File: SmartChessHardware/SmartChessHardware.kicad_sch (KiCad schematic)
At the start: 26 parts, among them IC1 Pi-Zero-UART, IC2 Arduino_UNO_R3, IC3 MCP23017x-x-SO, J1 Barrel_Jack

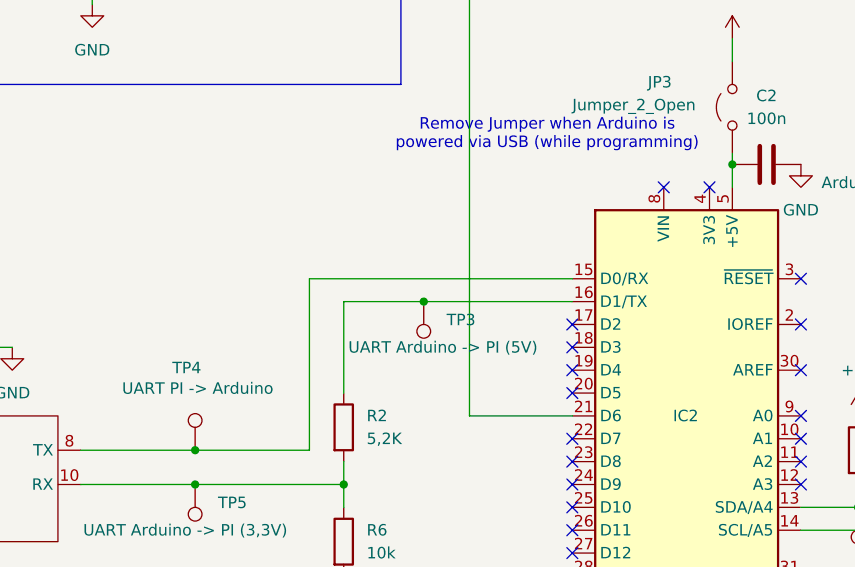
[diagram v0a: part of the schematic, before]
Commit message: Added jumper to disconnect UART
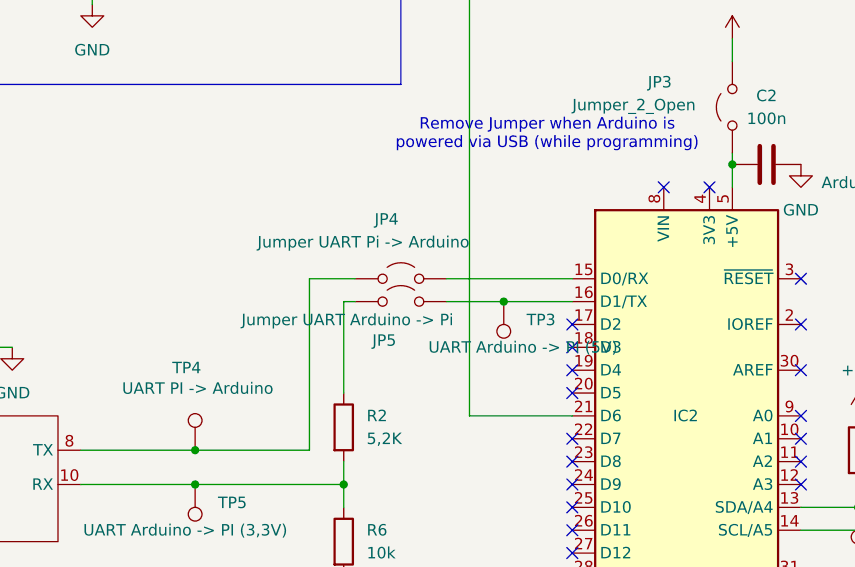
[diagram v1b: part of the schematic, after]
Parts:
- added JP4: Jumper UART Pi -> Arduino, symbol Jumper:Jumper_2_Open
- added JP5: Jumper UART Arduino -> Pi, symbol Jumper:Jumper_2_Open
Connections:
- net at IC1.8 (TX), TP4.1: now also JP4.1 (A); no longer IC2.15 (D0/RX)
- net at IC2.16 (D1/TX), TP3.1: now also JP5.2 (B); no longer R2.1
- new net: JP5.1 (A), R2.1
- new net: IC2.15 (D0/RX), JP4.2 (B)
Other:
- moved on the sheet: TP3
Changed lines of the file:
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@@
 	)
 	(junction
-		(at 114.3 82.55)
+		(at 123.19 82.55)
 		(diameter 0)
 		(color 0 0 0 0)
@@
 	(wire
 		(pts
-			(xy 130.81 82.55) (xy 114.3 82.55)
+			(xy 130.81 82.55) (xy 123.19 82.55)
 		)
 		(stroke
@@
 	(wire
 		(pts
+			(xy 116.84 80.01) (xy 130.81 80.01)
+		)
+		(stroke
+			(width 0)
+			(type default)
+		)
+	)
+	(wire
+		(pts
 			(xy 128.27 113.03) (xy 128.27 135.89)
 		)
@@
 	(wire
 		(pts
-			(xy 101.6 80.01) (xy 130.81 80.01)
+			(xy 101.6 80.01) (xy 106.68 80.01)
 		)
 		(stroke
@@
 	(wire
 		(pts
-			(xy 114.3 82.55) (xy 105.41 82.55)
+			(xy 105.41 82.55) (xy 106.68 82.55)
 		)
 		(stroke
@@
 	(wire
 		(pts
+			(xy 116.84 82.55) (xy 123.19 82.55)
+		)
+		(stroke
+			(width 0)
+			(type default)
+		)
+	)
+	(wire
+		(pts
 			(xy 227.33 105.41) (xy 227.33 115.57)
 		)
@@
 	)
 	(symbol
+		(lib_id "Jumper:Jumper_2_Open")
+		(at 111.76 82.55 0)
+		(unit 1)
+		(body_style 1)
+		(exclude_from_sim no)
+		(in_bom yes)
+		(on_board yes)
+		(in_pos_files yes)
+		(dnp no)
+		(property "Reference" "JP5"
+			(at 111.252 86.868 0)
+			(show_name no)
+			(do_not_autoplace no)
+			(effects
+				(font
+					(size 1.27 1.27)
+				)
+				(justify right)
+			)
+		)
+		(property "Value" "Jumper UART Arduino -> Pi"
+			(at 117.602 84.582 0)
+			(show_name no)
+			(do_not_autoplace no)
+			(effects
+				(font
+					(size 1.27 1.27)
+				)
+				(justify right)
+			)
+		)
+		(property "Footprint" ""
+			(at 111.76 82.55 0)
+			(hide yes)
+			(show_name no)
+			(do_not_autoplace no)
+			(effects
+				(font
+					(size 1.27 1.27)
+				)
+			)
+		)
+		(property "Datasheet" ""
+			(at 111.76 82.55 0)
+			(hide yes)
+			(show_name no)
+			(do_not_autoplace no)
+			(effects
+				(font
+					(size 1.27 1.27)
+				)
+			)
+		)
+		(property "Description" "Jumper, 2-pole, open"
+			(at 111.76 82.55 0)
+			(hide yes)
+			(show_name no)
+			(do_not_autoplace no)
+			(effects
+				(font
+					(size 1.27 1.27)
+				)
+			)
+		)
+		(pin "1"
+		)
+		(pin "2"
+		)
+		(instances
+			(project "SmartChessHardware"
+				(path "/f14972b6-de47-451d-92ca-2832c545b949"
+					(reference "JP5")
+					(unit 1)
+				)
+			)
+		)
+	)
+	(symbol
 		(lib_id "Connector:TestPoint")
 		(at 88.9 102.87 180)
@@
 	)
 	(symbol
+		(lib_id "Jumper:Jumper_2_Open")
+		(at 111.76 80.01 0)
+		(unit 1)
+		(body_style 1)
+		(exclude_from_sim no)
+		(in_bom yes)
+		(on_board yes)
+		(in_pos_files yes)
+		(dnp no)
+		(property "Reference" "JP4"
+			(at 111.506 73.406 0)
+			(show_name no)
+			(do_not_autoplace no)
+			(effects
+				(font
+					(size 1.27 1.27)
+				)
+				(justify right)
+			)
+		)
+		(property "Value" "Jumper UART Pi -> Arduino"
+			(at 119.38 75.946 0)
+			(show_name no)
+			(do_not_autoplace no)
+			(effects
+				(font
+					(size 1.27 1.27)
+				)
+				(justify right)
+			)
+		)
+		(property "Footprint" ""
+			(at 111.76 80.01 0)
+			(hide yes)
+			(show_name no)
+			(do_not_autoplace no)
+			(effects
+				(font
+					(size 1.27 1.27)
+				)
+			)
+		)
+		(property "Datasheet" ""
+			(at 111.76 80.01 0)
+			(hide yes)
+			(show_name no)
+			(do_not_autoplace no)
+			(effects
+				(font
+					(size 1.27 1.27)
+				)
+			)
+		)
+		(property "Description" "Jumper, 2-pole, open"
+			(at 111.76 80.01 0)
+			(hide yes)
+			(show_name no)
+			(do_not_autoplace no)
+			(effects
+				(font
+					(size 1.27 1.27)
+				)
+			)
+		)
+		(pin "1"
+		)
+		(pin "2"
+		)
+		(instances
+			(project "SmartChessHardware"
+				(path "/f14972b6-de47-451d-92ca-2832c545b949"
+					(reference "JP4")
+					(unit 1)
+				)
+			)
+		)
+	)
+	(symbol
 		(lib_id "MCU_Module:Arduino_UNO_R3")
 		(at 143.51 95.25 0)
@@
 	(symbol
 		(lib_id "Connector:TestPoint")
-		(at 114.3 82.55 180)
+		(at 123.19 82.55 180)
 		(unit 1)
 		(body_style 1)
@@
 		(dnp no)
 		(property "Reference" "TP3"
-			(at 116.84 84.5819 0)
+			(at 125.73 84.5819 0)
 			(show_name no)
 			(do_not_autoplace no)
@@
 		)
 		(property "Value" "UART Arduino -> PI (5V)"
-			(at 105.918 87.63 0)
+			(at 114.808 87.63 0)
 			(show_name no)
 			(do_not_autoplace no)
@@
 		)
 		(property "Footprint" ""
-			(at 109.22 82.55 0)
+			(at 118.11 82.55 0)
 			(hide yes)
 			(show_name no)
@@
 		)
 		(property "Datasheet" ""
-			(at 109.22 82.55 0)
+			(at 118.11 82.55 0)
 			(hide yes)
 			(show_name no)
@@
 		)
 		(property "Description" "test point"
-			(at 114.3 82.55 0)
+			(at 123.19 82.55 0)
 			(hide yes)
 			(show_name no)

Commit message: Assigned Footprints
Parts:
- C1, C2, C3, C4: footprint (none) -> Capacitor_SMD:C_0603_1608Metric
- F1: footprint (none) -> Fuse:Fuse_0603_1608Metric
- J1: footprint (none) -> Connector_BarrelJack:BarrelJack_GCT_DCJ200-10-A_Horizontal
- JP1, JP2, JP3, JP4, JP5: footprint (none) -> Connector_PinHeader_1.00mm:PinHeader_1x02_P1.00mm_Vertical
- R1, R2, R3, R4, R5, R6: footprint (none) -> Resistor_SMD:R_0603_1608Metric
- TP1, TP2, TP3, TP4, TP5, TP6, TP7, TP8: footprint (none) -> TestPoint:TestPoint_THTPad_D2.0mm_Drill1.0mm
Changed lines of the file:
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@@
 			)
 		)
-		(property "Footprint" ""
+		(property "Footprint" "Connector_PinHeader_1.00mm:PinHeader_1x02_P1.00mm_Vertical"
 			(at 111.76 82.55 0)
 			(hide yes)
@@
 			)
 		)
-		(property "Footprint" ""
+		(property "Footprint" "TestPoint:TestPoint_THTPad_D2.0mm_Drill1.0mm"
 			(at 83.82 102.87 0)
 			(hide yes)
@@
 			)
 		)
-		(property "Footprint" ""
+		(property "Footprint" "TestPoint:TestPoint_THTPad_D2.0mm_Drill1.0mm"
 			(at 157.48 105.41 0)
 			(hide yes)
@@
 			)
 		)
-		(property "Footprint" ""
+		(property "Footprint" "Fuse:Fuse_0603_1608Metric"
 			(at 82.55 41.148 90)
 			(hide yes)
@@
 			)
 		)
-		(property "Footprint" ""
+		(property "Footprint" "TestPoint:TestPoint_THTPad_D2.0mm_Drill1.0mm"
 			(at 93.98 99.06 0)
 			(hide yes)
@@
 			)
 		)
-		(property "Footprint" ""
+		(property "Footprint" "Resistor_SMD:R_0603_1608Metric"
 			(at 103.632 96.52 90)
 			(hide yes)
@@
 			)
 		)
-		(property "Footprint" ""
+		(property "Footprint" "Connector_PinHeader_1.00mm:PinHeader_1x02_P1.00mm_Vertical"
 			(at 111.76 80.01 0)
 			(hide yes)
@@
 			)
 		)
-		(property "Footprint" ""
+		(property "Footprint" "Connector_PinHeader_1.00mm:PinHeader_1x02_P1.00mm_Vertical"
 			(at 148.59 60.96 0)
 			(hide yes)
@@
 			)
 		)
-		(property "Footprint" ""
+		(property "Footprint" "Connector_BarrelJack:BarrelJack_GCT_DCJ200-10-A_Horizontal"
 			(at 67.31 37.846 0)
 			(hide yes)
@@
 			)
 		)
-		(property "Footprint" ""
+		(property "Footprint" "Resistor_SMD:R_0603_1608Metric"
 			(at 152.4 42.418 90)
 			(hide yes)
@@
 			)
 		)
-		(property "Footprint" ""
+		(property "Footprint" "TestPoint:TestPoint_THTPad_D2.0mm_Drill1.0mm"
 			(at 73.66 34.29 0)
 			(hide yes)
@@
 			)
 		)
-		(property "Footprint" ""
+		(property "Footprint" "Resistor_SMD:R_0603_1608Metric"
 			(at 160.782 99.06 90)
 			(hide yes)
@@
 			)
 		)
-		(property "Footprint" ""
+		(property "Footprint" "Resistor_SMD:R_0603_1608Metric"
 			(at 170.942 99.06 90)
 			(hide yes)
@@
 			)
 		)
-		(property "Footprint" ""
+		(property "Footprint" "TestPoint:TestPoint_THTPad_D2.0mm_Drill1.0mm"
 			(at 102.87 44.45 0)
 			(hide yes)
@@
 			)
 		)
-		(property "Footprint" ""
+		(property "Footprint" "TestPoint:TestPoint_THTPad_D2.0mm_Drill1.0mm"
 			(at 171.45 116.84 0)
 			(hide yes)
@@
 			)
 		)
-		(property "Footprint" ""
+		(property "Footprint" "Connector_PinHeader_1.00mm:PinHeader_1x02_P1.00mm_Vertical"
 			(at 203.2 54.61 0)
 			(hide yes)
@@
 			)
 		)
-		(property "Footprint" ""
+		(property "Footprint" "Capacitor_SMD:C_0603_1608Metric"
 			(at 78.4352 46.99 0)
 			(hide yes)
@@
 			)
 		)
-		(property "Footprint" ""
+		(property "Footprint" "Capacitor_SMD:C_0603_1608Metric"
 			(at 210.82 66.3448 0)
 			(hide yes)
@@
 			)
 		)
-		(property "Footprint" ""
+		(property "Footprint" "TestPoint:TestPoint_THTPad_D2.0mm_Drill1.0mm"
 			(at 118.11 82.55 0)
 			(hide yes)
@@
 			)
 		)
-		(property "Footprint" ""
+		(property "Footprint" "Connector_PinHeader_1.00mm:PinHeader_1x02_P1.00mm_Vertical"
 			(at 92.71 39.37 0)
 			(hide yes)
@@
 			)
 		)
-		(property "Footprint" ""
+		(property "Footprint" "Resistor_SMD:R_0603_1608Metric"
 			(at 184.912 99.06 90)
 			(hide yes)
@@
 			)
 		)
-		(property "Footprint" ""
+		(property "Footprint" "TestPoint:TestPoint_THTPad_D2.0mm_Drill1.0mm"
 			(at 167.64 107.95 0)
 			(hide yes)
@@
 			)
 		)
-		(property "Footprint" ""
+		(property "Footprint" "Resistor_SMD:R_0603_1608Metric"
 			(at 103.632 109.22 90)
 			(hide yes)
@@
 			)
 		)
-		(property "Footprint" ""
+		(property "Footprint" "Capacitor_SMD:C_0603_1608Metric"
 			(at 54.61 91.1352 0)
 			(hide yes)
@@
 			)
 		)
-		(property "Footprint" ""
+		(property "Footprint" "Capacitor_SMD:C_0603_1608Metric"
 			(at 156.21 66.3448 0)
 			(hide yes)

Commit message: Reworked supply circuit
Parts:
- added D1: 1N4001, Diode_THT:D_DO-41_SOD81_P10.16mm_Horizontal, symbol Diode:1N4001
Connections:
- net at F1.1, J1.2: no longer C1.1
- net at JP1.1 (A): now also C1.1, D1.1 (K); no longer F1.2
- new net: D1.2 (A), F1.2
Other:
- moved on the sheet: C1, J1, JP1, TP1, TP2

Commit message: Added sheept for print
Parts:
- removed D1: 1N4001, Diode_THT:D_DO-41_SOD81_P10.16mm_Horizontal, symbol Diode:1N4001
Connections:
- net at C1.1, JP1.1 (A): now also F1.2
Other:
- added sheet PrintAndDrills (print_and_drills.kicad_sch)
- moved on the sheet: C1, JP1, TP2

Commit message: Layout wip
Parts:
- C1: footprint Capacitor_SMD:C_0603_1608Metric -> Capacitor_THT:CP_Radial_D6.3mm_P2.50mm
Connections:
- net +5V: now also IC1.4 (+5V); no longer IC1. (+5V)
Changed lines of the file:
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@@
 			)
 		)
-		(pin ""
+		(pin "4"
 		)
 		(pin "6"
@@
 			)
 		)
-		(property "Footprint" "Capacitor_SMD:C_0603_1608Metric"
+		(property "Footprint" "Capacitor_THT:CP_Radial_D6.3mm_P2.50mm"
 			(at 55.5752 46.99 0)
 			(hide yes)
